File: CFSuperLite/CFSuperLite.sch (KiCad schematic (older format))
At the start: 24 parts, among them J1 IDE to CF adapter, J2 CF Adapter Power, J3 Bus_ISA_8bit, SW1 Options, U1 BIOS FLASH, U2 74HCT245, U3 ATF/GAL16V8x-15, U4 DS1315, Y1 32.768 KHz

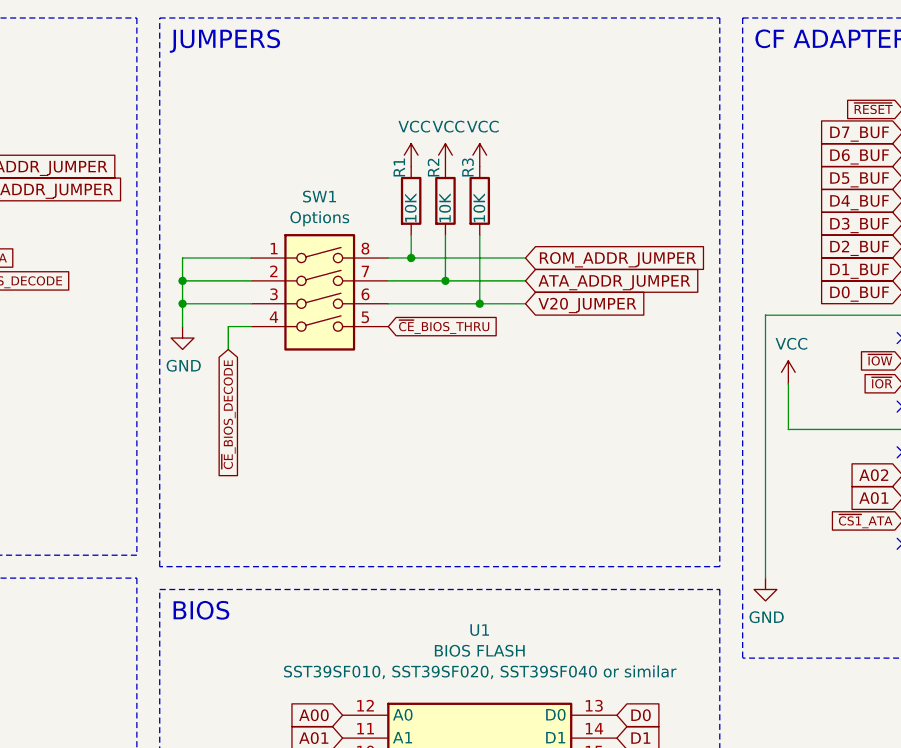
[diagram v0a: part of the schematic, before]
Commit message: CFSuperLite: Add option to use 3-way DIP switch and 0 ohm resistor for assembly variation without RTC parts.
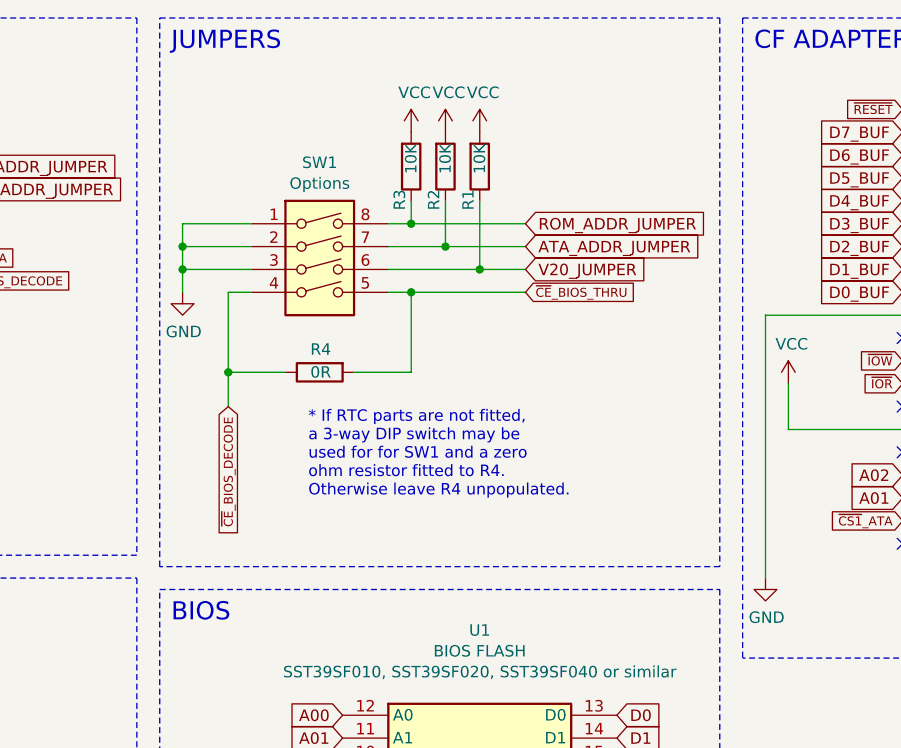
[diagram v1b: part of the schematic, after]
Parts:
- added R4: 0R, Resistor_SMD:R_1206_3216Metric, symbol Device:R
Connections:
- net ATA_ADDR_JUMPER: now also R2.1; no longer R2.2
- net ROM_ADDR_JUMPER: now also R1.1; no longer R1.2
- net V20_JUMPER: now also R3.1; no longer R3.2
- net VCC: now also R1.2, R2.2, R3.2; no longer R1.1, R2.1, R3.1
- net ~CE~_BIOS_DECODE: now also R4.1
- net ~CE~_BIOS_THRU: now also R4.2
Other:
- note added: "* If RTC parts are not fitted, \na 3-way DIP switch may be \nused for for SW1 and a zero \nohm resistor fitted to R4. \nOtherwise leave R4 unpopulated."
- moved on the sheet: R1, R2, R3, SW1
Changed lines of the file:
@@
 L power:VCC #PWR0114
 U 1 1 60CA7D3F
-P 7000 1200
-F 0 "#PWR0114" H 7000 1050 50  0001 C CNN
-F 1 "VCC" H 7015 1373 50  0000 C CNN
-F 2 "" H 7000 1200 50  0001 C CNN
-F 3 "" H 7000 1200 50  0001 C CNN
-	1    7000 1200
-	1    0    0    -1
-$EndComp
-Text GLabel 7500 1700 2    50   Input ~ 0
+P 7000 1050
+F 0 "#PWR0114" H 7000 900 50  0001 C CNN
+F 1 "VCC" H 7015 1223 50  0000 C CNN
+F 2 "" H 7000 1050 50  0001 C CNN
+F 3 "" H 7000 1050 50  0001 C CNN
+	1    7000 1050
+	1    0    0    -1
+$EndComp
+Text GLabel 7500 1550 2    50   Input ~ 0
 ATA_ADDR_JUMPER
-Text GLabel 7500 1600 2    50   Input ~ 0
+Text GLabel 7500 1450 2    50   Input ~ 0
 ROM_ADDR_JUMPER
 $Comp
 L power:GND #PWR0138
 U 1 1 60CBC847
-P 6000 1900
-F 0 "#PWR0138" H 6000 1650 50  0001 C CNN
-F 1 "GND" H 6005 1727 50  0000 C CNN
-F 2 "" H 6000 1900 50  0001 C CNN
-F 3 "" H 6000 1900 50  0001 C CNN
-	1    6000 1900
-	1    0    0    -1
-$EndComp
-Text GLabel 6200 2000 3    39   Input ~ 0
+P 6000 1750
+F 0 "#PWR0138" H 6000 1500 50  0001 C CNN
+F 1 "GND" H 6005 1577 50  0000 C CNN
+F 2 "" H 6000 1750 50  0001 C CNN
+F 3 "" H 6000 1750 50  0001 C CNN
+	1    6000 1750
+	1    0    0    -1
+$EndComp
+Text GLabel 6200 2250 3    39   Input ~ 0
 ~CE~_BIOS_DECODE
-Text GLabel 7500 1800 2    50   Input ~ 0
+Text GLabel 7500 1650 2    50   Input ~ 0
 V20_JUMPER
-$Comp
-L Switch:SW_DIP_x04 SW1
-U 1 1 61651524
-P 6600 1800
-F 0 "SW1" H 6600 2267 50  0000 C CNN
-F 1 "Options" H 6600 2176 50  0000 C CNN
-F 2 "Button_Switch_THT:SW_DIP_SPSTx04_Slide_9.78x12.34mm_W7.62mm_P2.54mm" H 6600 1800 50  0001 C CNN
-F 3 "~" H 6600 1800 50  0001 C CNN
-F 4 "C15781" H 6600 1800 50  0001 C CNN "LCSC"
-F 5 "C15781, C99418, C319060, C47207" H 6600 1800 50  0001 C CNN "Part options"
-	1    6600 1800
-	1    0    0    -1
-$EndComp
-Wire Wire Line
-	6900 1600 7000 1600
-Wire Wire Line
-	7000 1600 7000 1500
-Text GLabel 6900 1900 2    39   Input ~ 0
+Wire Wire Line
+	6900 1450 7000 1450
+Wire Wire Line
+	7000 1450 7000 1350
+Text GLabel 7500 1750 2    39   Input ~ 0
 ~CE~_BIOS_THRU
 Wire Wire Line
-	7500 1800 7300 1800
-Wire Wire Line
-	6900 1700 7150 1700
-Wire Wire Line
-	7500 1600 7000 1600
-Connection ~ 7000 1600
-Wire Wire Line
-	7150 1700 7150 1500
-Connection ~ 7150 1700
-Wire Wire Line
-	7150 1700 7500 1700
-Wire Wire Line
-	7300 1800 7300 1500
-Connection ~ 7300 1800
-Wire Wire Line
-	7300 1800 6900 1800
+	7500 1650 7300 1650
+Wire Wire Line
+	6900 1550 7150 1550
+Wire Wire Line
+	7500 1450 7000 1450
+Connection ~ 7000 1450
+Wire Wire Line
+	7150 1550 7150 1350
+Connection ~ 7150 1550
+Wire Wire Line
+	7150 1550 7500 1550
+Wire Wire Line
+	7300 1650 7300 1350
+Connection ~ 7300 1650
+Wire Wire Line
+	7300 1650 6900 1650
 $Comp
 L Device:R R1
 U 1 1 61672F07
-P 7000 1350
-F 0 "R1" V 6950 1450 50  0000 L CNN
-F 1 "10K" V 7000 1250 50  0000 L CNN
-F 2 "Resistor_SMD:R_1206_3216Metric" V 6930 1350 50  0001 C CNN
-F 3 "~" H 7000 1350 50  0001 C CNN
-F 4 "C17902" H 7000 1350 50  0001 C CNN "LCSC"
-	1    7000 1350
-	1    0    0    -1
+P 7000 1200
+F 0 "R1" V 7250 1300 50  0000 L CNN
+F 1 "10K" V 7000 1100 50  0000 L CNN
+F 2 "Resistor_SMD:R_1206_3216Metric" V 6930 1200 50  0001 C CNN
+F 3 "~" H 7000 1200 50  0001 C CNN
+F 4 "C17902" H 7000 1200 50  0001 C CNN "LCSC"
+	1    7000 1200
+	1    0    0    1
 $EndComp
 $Comp
 L power:VCC #PWR0104
 U 1 1 6167596C
-P 7150 1200
-F 0 "#PWR0104" H 7150 1050 50  0001 C CNN
-F 1 "VCC" H 7165 1373 50  0000 C CNN
-F 2 "" H 7150 1200 50  0001 C CNN
-F 3 "" H 7150 1200 50  0001 C CNN
-	1    7150 1200
+P 7150 1050
+F 0 "#PWR0104" H 7150 900 50  0001 C CNN
+F 1 "VCC" H 7165 1223 50  0000 C CNN
+F 2 "" H 7150 1050 50  0001 C CNN
+F 3 "" H 7150 1050 50  0001 C CNN
+	1    7150 1050
 	1    0    0    -1
 $EndComp
@@
 L Device:R R2
 U 1 1 61675EE5
-P 7150 1350
-F 0 "R2" V 7100 1450 50  0000 L CNN
-F 1 "10K" V 7150 1250 50  0000 L CNN
-F 2 "Resistor_SMD:R_1206_3216Metric" V 7080 1350 50  0001 C CNN
-F 3 "~" H 7150 1350 50  0001 C CNN
-F 4 "C17902" H 7150 1350 50  0001 C CNN "LCSC"
-	1    7150 1350
-	1    0    0    -1
+P 7150 1200
+F 0 "R2" V 7100 1300 50  0000 L CNN
+F 1 "10K" V 7150 1100 50  0000 L CNN
+F 2 "Resistor_SMD:R_1206_3216Metric" V 7080 1200 50  0001 C CNN
+F 3 "~" H 7150 1200 50  0001 C CNN
+F 4 "C17902" H 7150 1200 50  0001 C CNN "LCSC"
+	1    7150 1200
+	1    0    0    1
 $EndComp
 $Comp
 L power:VCC #PWR0130
 U 1 1 6167A124
-P 7300 1200
-F 0 "#PWR0130" H 7300 1050 50  0001 C CNN
-F 1 "VCC" H 7315 1373 50  0000 C CNN
-F 2 "" H 7300 1200 50  0001 C CNN
-F 3 "" H 7300 1200 50  0001 C CNN
-	1    7300 1200
-	1    0    0    -1
-$EndComp
-$Comp
-L Device:R R3
-U 1 1 6167A6BD
-P 7300 1350
-F 0 "R3" V 7250 1450 50  0000 L CNN
-F 1 "10K" V 7300 1250 50  0000 L CNN
-F 2 "Resistor_SMD:R_1206_3216Metric" V 7230 1350 50  0001 C CNN
-F 3 "~" H 7300 1350 50  0001 C CNN
-F 4 "C17902" H 7300 1350 50  0001 C CNN "LCSC"
-	1    7300 1350
-	1    0    0    -1
-$EndComp
-Wire Wire Line
-	6300 1900 6200 1900
-Wire Wire Line
-	6200 1900 6200 2000
-Wire Wire Line
-	6300 1600 6000 1600
-Wire Wire Line
-	6000 1600 6000 1700
-Wire Wire Line
-	6300 1800 6000 1800
-Connection ~ 6000 1800
-Wire Wire Line
-	6000 1800 6000 1900
-Wire Wire Line
-	6300 1700 6000 1700
-Connection ~ 6000 1700
-Wire Wire Line
-	6000 1700 6000 1800
+P 7300 1050
+F 0 "#PWR0130" H 7300 900 50  0001 C CNN
+F 1 "VCC" H 7315 1223 50  0000 C CNN
+F 2 "" H 7300 1050 50  0001 C CNN
+F 3 "" H 7300 1050 50  0001 C CNN
+	1    7300 1050
+	1    0    0    -1
+$EndComp
+Wire Wire Line
+	6300 1750 6200 1750
+Wire Wire Line
+	6200 1750 6200 2100
+Wire Wire Line
+	6300 1450 6000 1450
+Wire Wire Line
+	6000 1450 6000 1550
+Wire Wire Line
+	6300 1650 6000 1650
+Connection ~ 6000 1650
+Wire Wire Line
+	6000 1650 6000 1750
+Wire Wire Line
+	6300 1550 6000 1550
+Connection ~ 6000 1550
+Wire Wire Line
+	6000 1550 6000 1650
 Text GLabel 4100 6800 2    39   Input ~ 0
 ~CE~_BIOS_THRU
@@
 A17
 $Comp
-L power:GND #PWR?
+L power:GND #PWR02
 U 1 1 6161E5C8
 P 6600 7200
-F 0 "#PWR?" H 6600 6950 50  0001 C CNN
+F 0 "#PWR02" H 6600 6950 50  0001 C CNN
 F 1 "GND" H 6605 7027 50  0000 C CNN
 F 2 "" H 6600 7200 50  0001 C CNN
@@
 $EndComp
 $Comp
-L power:VCC #PWR?
+L power:VCC #PWR01
 U 1 1 6161E5D2
 P 6600 6900
-F 0 "#PWR?" H 6600 6750 50  0001 C CNN
+F 0 "#PWR01" H 6600 6750 50  0001 C CNN
 F 1 "VCC" H 6615 7073 50  0000 C CNN
 F 2 "" H 6600 6900 50  0001 C CNN
@@
 	1    0    0    -1
 $EndComp
+Wire Wire Line
+	6900 1750 7000 1750
+Wire Wire Line
+	6450 2100 6200 2100
+Connection ~ 6200 2100
+Wire Wire Line
+	6200 2100 6200 2250
+Wire Wire Line
+	6750 2100 7000 2100
+Wire Wire Line
+	7000 2100 7000 1750
+Connection ~ 7000 1750
+Wire Wire Line
+	7000 1750 7500 1750
+$Comp
+L Device:R R4
+U 1 1 6164AD42
+P 6600 2100
+F 0 "R4" V 6500 2050 50  0000 L CNN
+F 1 "0R" V 6600 2050 50  0000 L CNN
+F 2 "Resistor_SMD:R_1206_3216Metric" V 6530 2100 50  0001 C CNN
+F 3 "~" H 6600 2100 50  0001 C CNN
+F 4 "C17888" H 6600 2100 50  0001 C CNN "LCSC"
+	1    6600 2100
+	0    -1   1    0
+$EndComp
+Text Notes 6550 2650 0    50   ~ 0
+* If RTC parts are not fitted, \na 3-way DIP switch may be \nused for for SW1 and a zero \nohm resistor fitted to R4. \nOtherwise leave R4 unpopulated.
+$Comp
+L Switch:SW_DIP_x04 SW1
+U 1 1 61651524
+P 6600 1650
+F 0 "SW1" H 6600 2117 50  0000 C CNN
+F 1 "Options" H 6600 2026 50  0000 C CNN
+F 2 "Button_Switch_THT:SW_DIP_SPSTx04_Slide_9.78x12.34mm_W7.62mm_P2.54mm" H 6600 1650 50  0001 C CNN
+F 3 "~" H 6600 1650 50  0001 C CNN
+F 4 "C15781" H 6600 1650 50  0001 C CNN "LCSC"
+F 5 "C15781, C99418, C319060, C47207" H 6600 1650 50  0001 C CNN "Part options"
+	1    6600 1650
+	1    0    0    -1
+$EndComp
+$Comp
+L Device:R R3
+U 1 1 6167A6BD
+P 7300 1200
+F 0 "R3" V 6950 1300 50  0000 L CNN
+F 1 "10K" V 7300 1100 50  0000 L CNN
+F 2 "Resistor_SMD:R_1206_3216Metric" V 7230 1200 50  0001 C CNN
+F 3 "~" H 7300 1200 50  0001 C CNN
+F 4 "C17902" H 7300 1200 50  0001 C CNN "LCSC"
+	1    7300 1200
+	1    0    0    1
+$EndComp
 $EndSCHEMATC
